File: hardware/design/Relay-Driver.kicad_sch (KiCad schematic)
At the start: 8 parts, among them K8501 G5LE-1, Q8501 2N3906, Q8502 2N3904

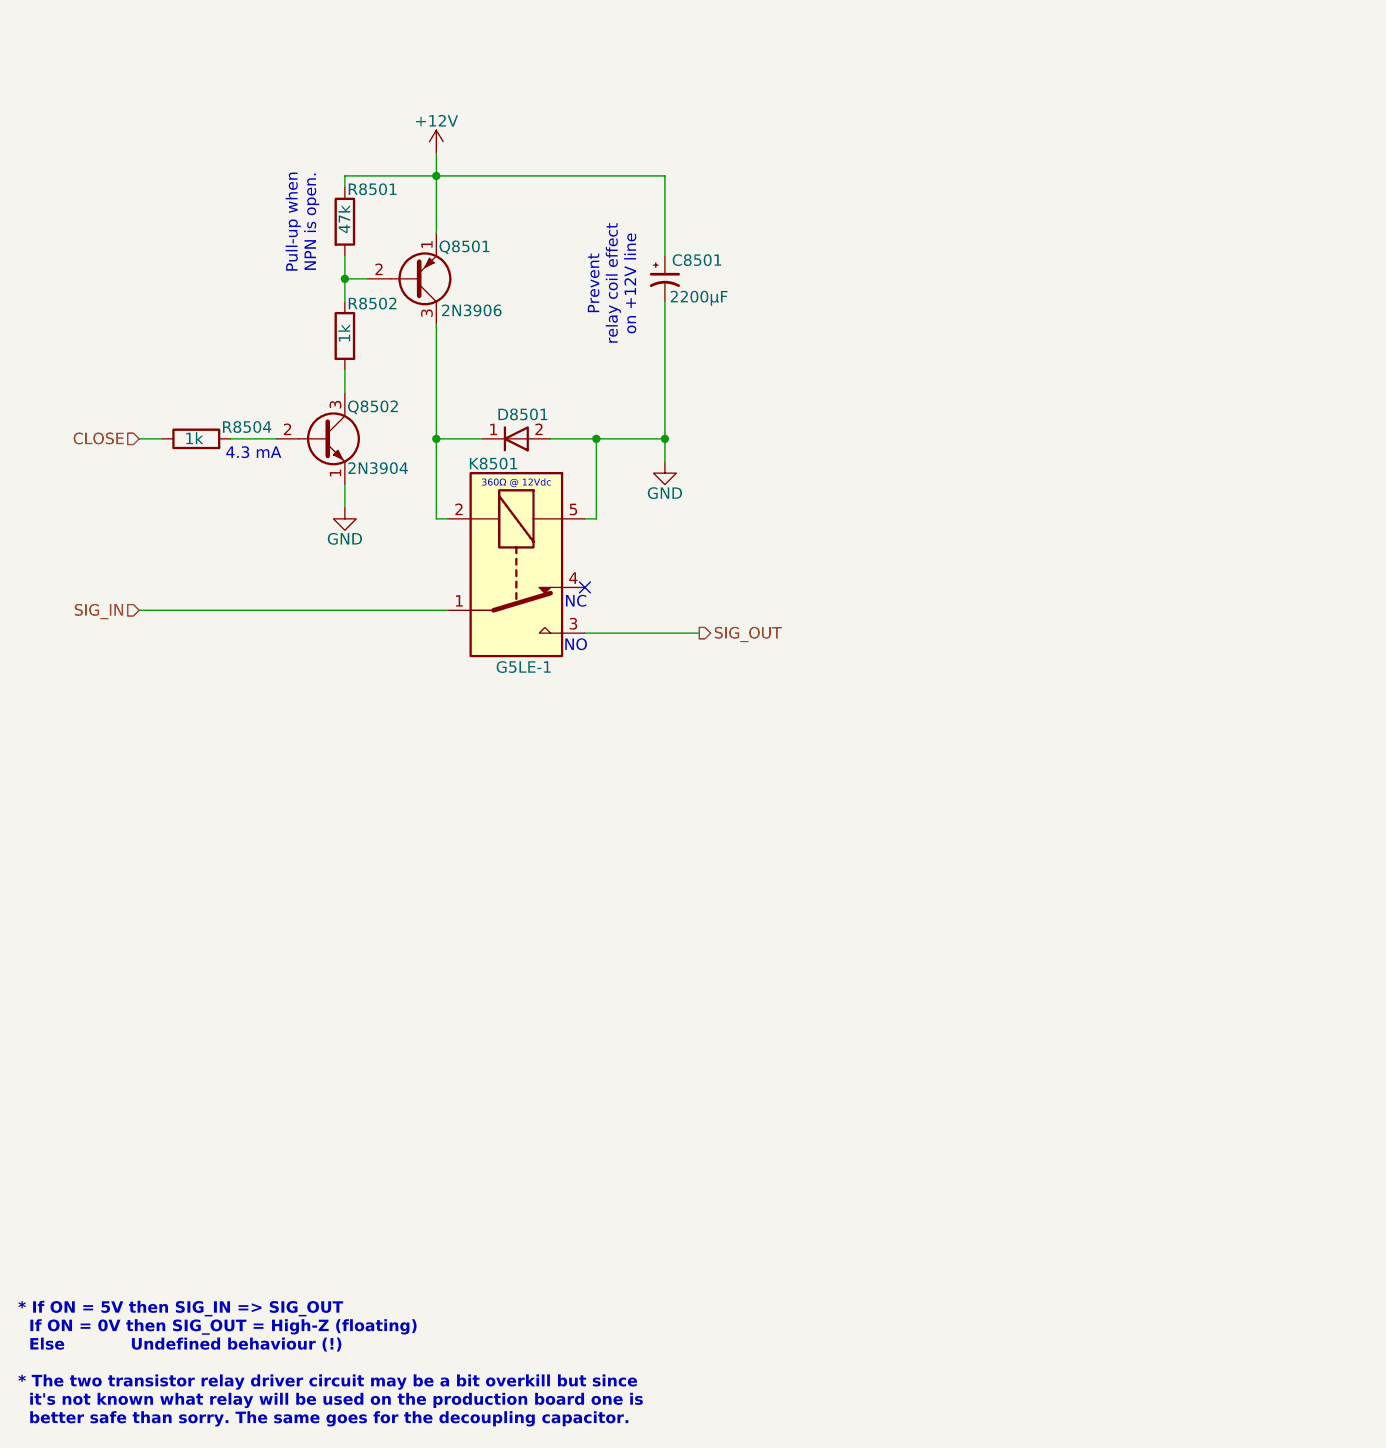
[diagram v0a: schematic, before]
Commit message: Simulating alternative power supply
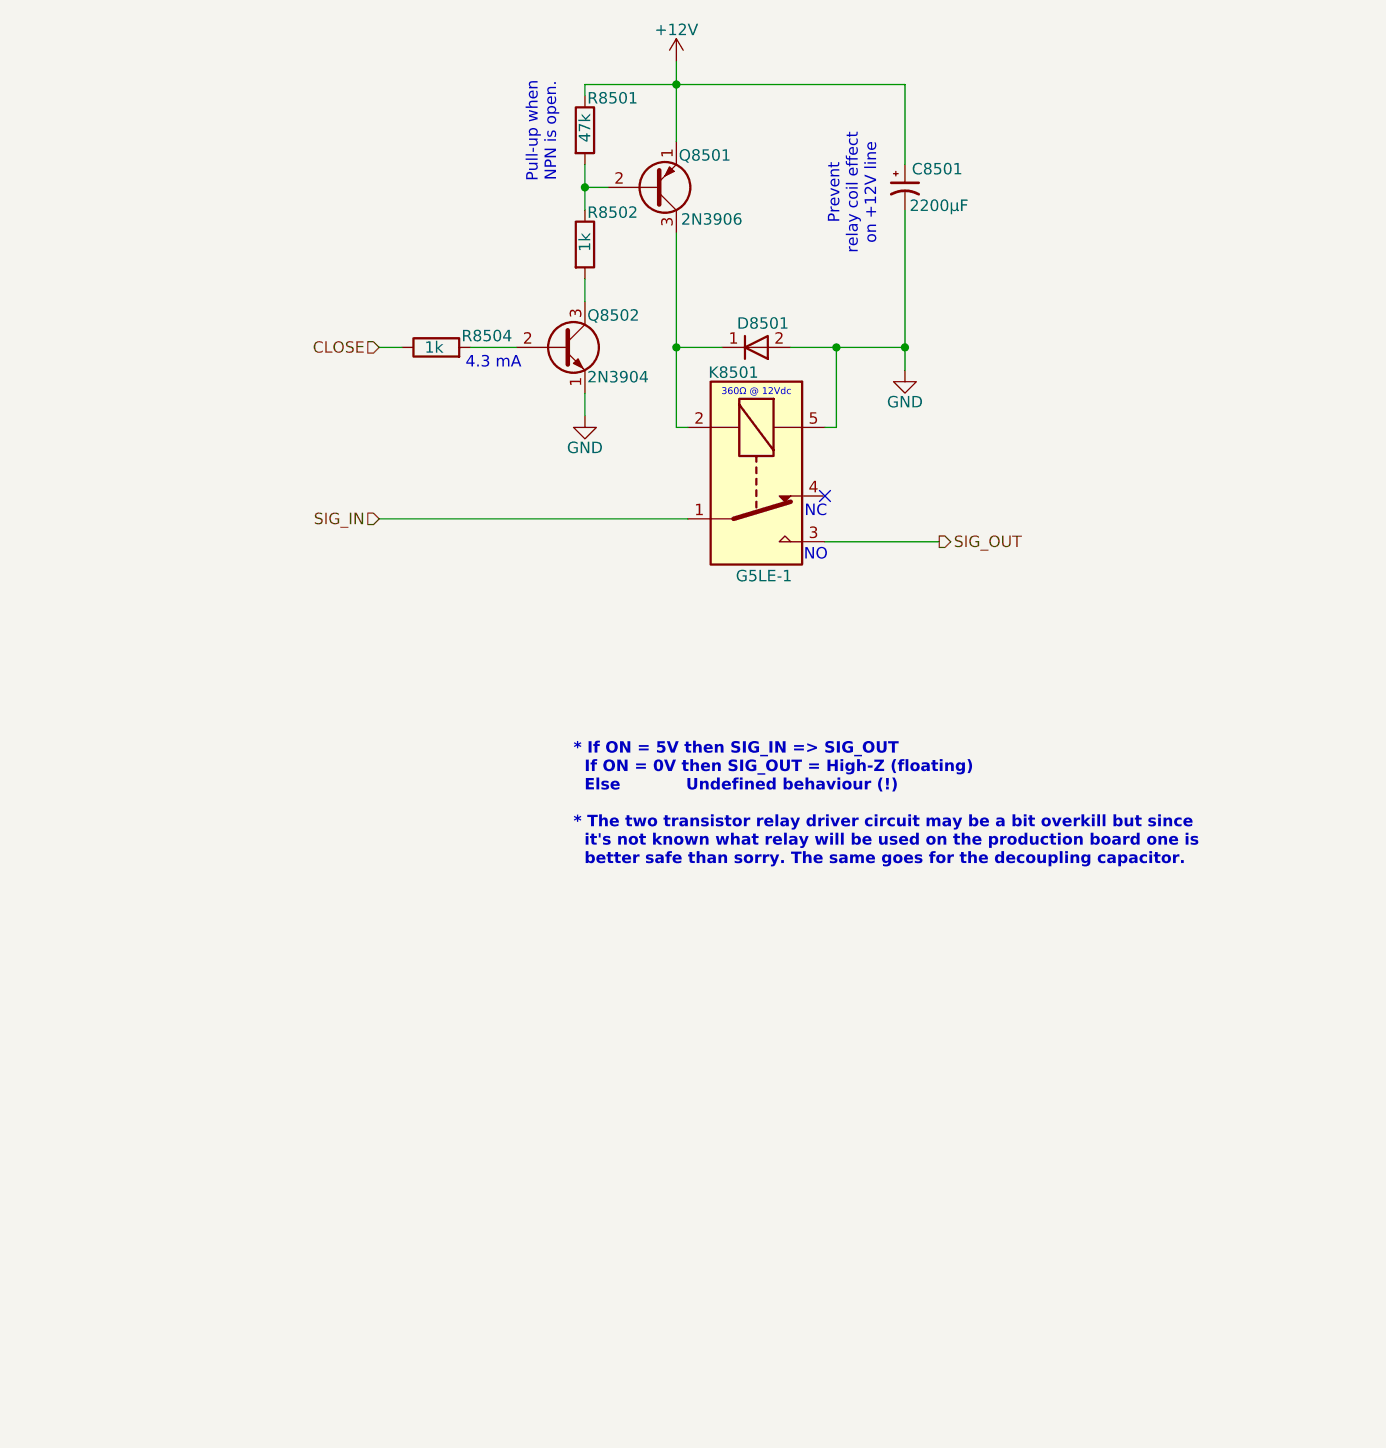
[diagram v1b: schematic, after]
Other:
- moved on the sheet: C8501, D8501, K8501, Q8501, Q8502, R8501, R8502, R8504
